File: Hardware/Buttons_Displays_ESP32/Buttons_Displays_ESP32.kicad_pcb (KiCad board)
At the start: 2 copper layers, 24 parts, among them J1 1778612, J2 1778612, J3 1778612, J4 1778612, J5 i2c, J6 USB_C_Receptacle_USB2.0_16P, SW1 SW_Push, SW2 SW_Push, U1 ESP32-S3-WROOM-1, U2 USBLC6-2P6

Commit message: pcb schermpjes af
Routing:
- net sda: track 14.4 -> 31.5 mm, vias 1 -> 2
- net scl: track 13.8 -> 25.0 mm, vias 1 -> 2
- net GPIO4: track 40.4 -> 29.3 mm, vias 1 -> 2
- net GND: track 0.00 -> 1.19 mm, vias 0 -> 142

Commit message: kleine aanpassingen
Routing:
- net GND: vias 142 -> 138
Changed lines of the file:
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@@
-	)
-	(via
-		(at 158.5 88.11)
-		(size 0.6)
-		(drill 0.3)
-		(layers "F.Cu" "B.Cu")
-		(free yes)
-		(net 2)
 	)
 	(via
@@
 	)
 	(via
-		(at 158.55 89.89)
-		(size 0.6)
-		(drill 0.3)
-		(layers "F.Cu" "B.Cu")
-		(free yes)
-		(net 2)
-	)
-	(via
 		(at 159.75 86.86)
 		(size 0.6)
@@
 	)
 	(via
-		(at 158.55 92.39)
-		(size 0.6)
-		(drill 0.3)
-		(layers "F.Cu" "B.Cu")
-		(free yes)
-		(net 2)
-	)
-	(via
 		(at 153.5 93.75)
 		(size 0.6)
@@
 		(size 0.6)
 		(drill 0.3)
-		(layers "F.Cu" "B.Cu")
-		(free yes)
-		(net 2)
-	)
-	(via
-		(at 158.5 85.61)
-		(size 0.6)
-		(drill 0.3)

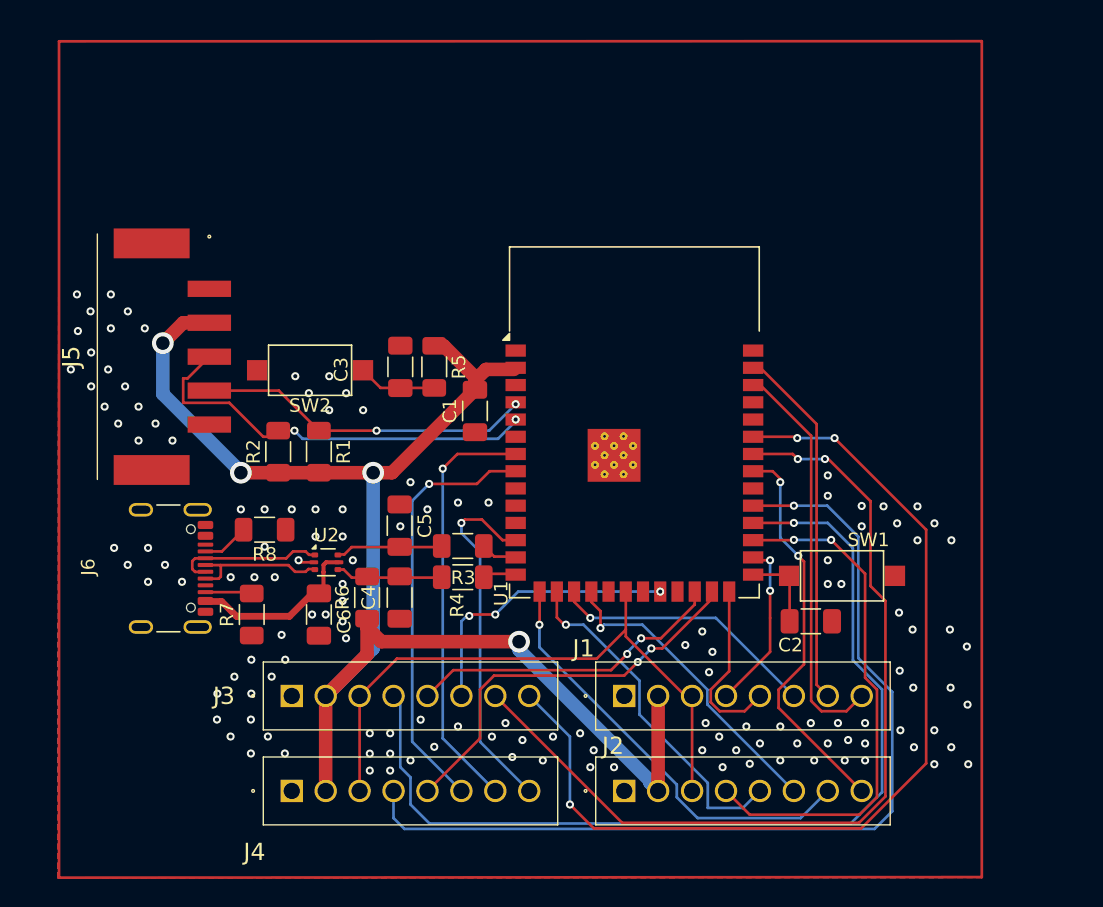
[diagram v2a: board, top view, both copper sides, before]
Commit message: mounting holes
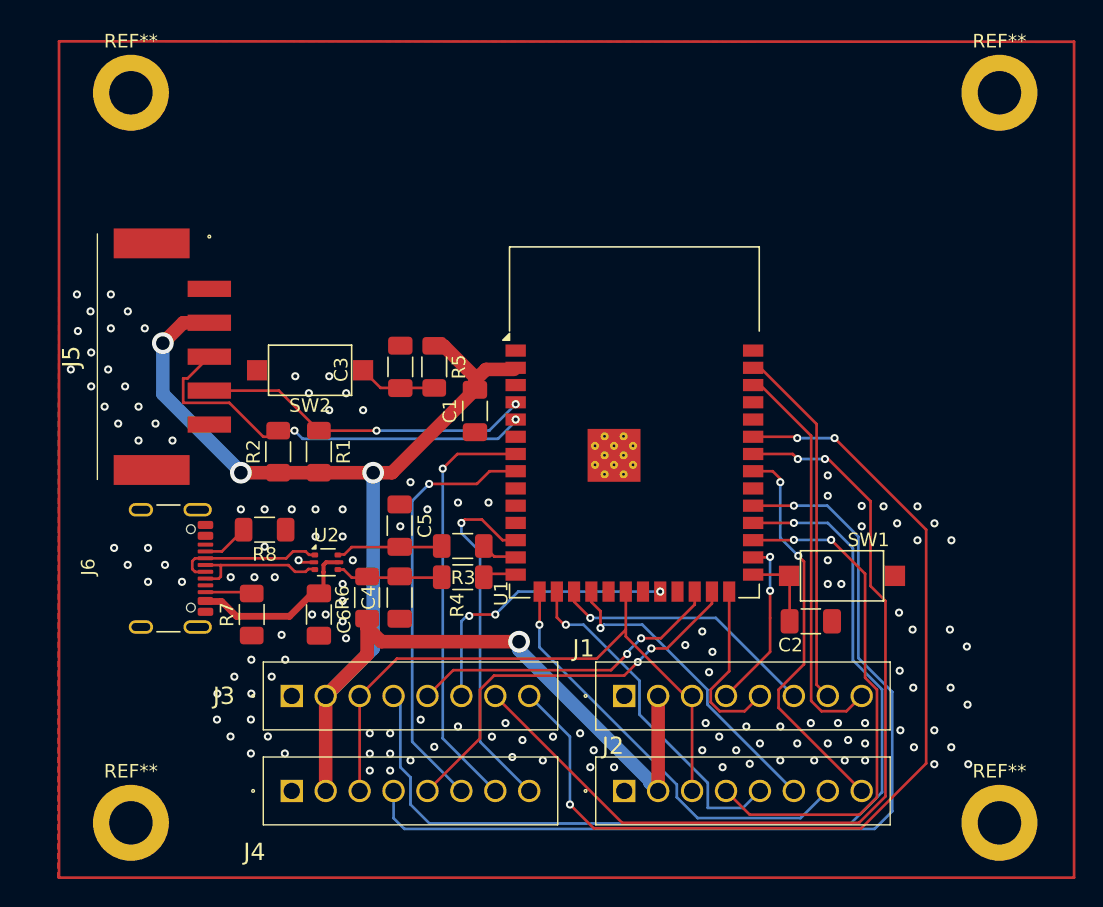
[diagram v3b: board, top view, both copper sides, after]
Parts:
- added REF**: MountingHole_3.2mm_M3_DIN965_Pad, MountingHole:MountingHole_3.2mm_M3_DIN965_Pad, F.Cu at (163.4, 101.1)
- added REF**: MountingHole_3.2mm_M3_DIN965_Pad, MountingHole:MountingHole_3.2mm_M3_DIN965_Pad, F.Cu at (163.4, 47.3)
- added REF**: MountingHole_3.2mm_M3_DIN965_Pad, MountingHole:MountingHole_3.2mm_M3_DIN965_Pad, F.Cu at (99.4, 47.3)
- added REF**: MountingHole_3.2mm_M3_DIN965_Pad, MountingHole:MountingHole_3.2mm_M3_DIN965_Pad, F.Cu at (99.4, 101.1)

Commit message: Update Buttons_Displays_ESP32.kicad_pcb
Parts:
- moved REF** 0.30 mm to (163.7, 101.1)
- moved REF** 0.30 mm to (163.7, 47.3)
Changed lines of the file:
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@@
 	(footprint "MountingHole:MountingHole_3.2mm_M3_DIN965_Pad"
 		(layer "F.Cu")
-		(at 163.4 101.1)
+		(at 163.7 101.1)
 		(descr "Mounting Hole 3.2mm, M3, DIN965")
 		(tags "mounting hole 3.2mm m3 din965")
@@
 			(at 0 -3.8 0)
 			(layer "F.SilkS")
+			(hide yes)
 			(effects
 				(font
@@
 	(footprint "MountingHole:MountingHole_3.2mm_M3_DIN965_Pad"
 		(layer "F.Cu")
-		(at 163.4 47.3)
+		(at 163.7 47.3)
 		(descr "Mounting Hole 3.2mm, M3, DIN965")
 		(tags "mounting hole 3.2mm m3 din965")
@@
 			(at 0 -3.8 0)
 			(layer "F.SilkS")
+			(hide yes)
 			(effects
 				(font
@@
 			(at 0 -3.8 0)
 			(layer "F.SilkS")
+			(hide yes)
 			(effects
 				(font
@@
 			(at 0 -3.8 0)
 			(layer "F.SilkS")
+			(hide yes)
 			(effects
 				(font
@@
 	)
 	(gr_line
-		(start 168.900024 43.54)
+		(start 94 105.18)
 		(end 94.1 43.51)
 		(stroke
@@
 	)
 	(gr_line
-		(start 94.1 105.14)
+		(start 168.900024 43.54)
 		(end 168.900024 105.14)
 		(stroke
@@
 	)
 	(gr_line
-		(start 168.900024 105.14)
+		(start 94.1 43.51)
 		(end 168.900024 43.54)
 		(stroke
@@
 	)
 	(gr_line
-		(start 94.1 43.51)
-		(end 94.1 105.14)
+		(start 168.900024 105.14)
+		(end 94 105.18)
 		(stroke
 			(width 0.2)

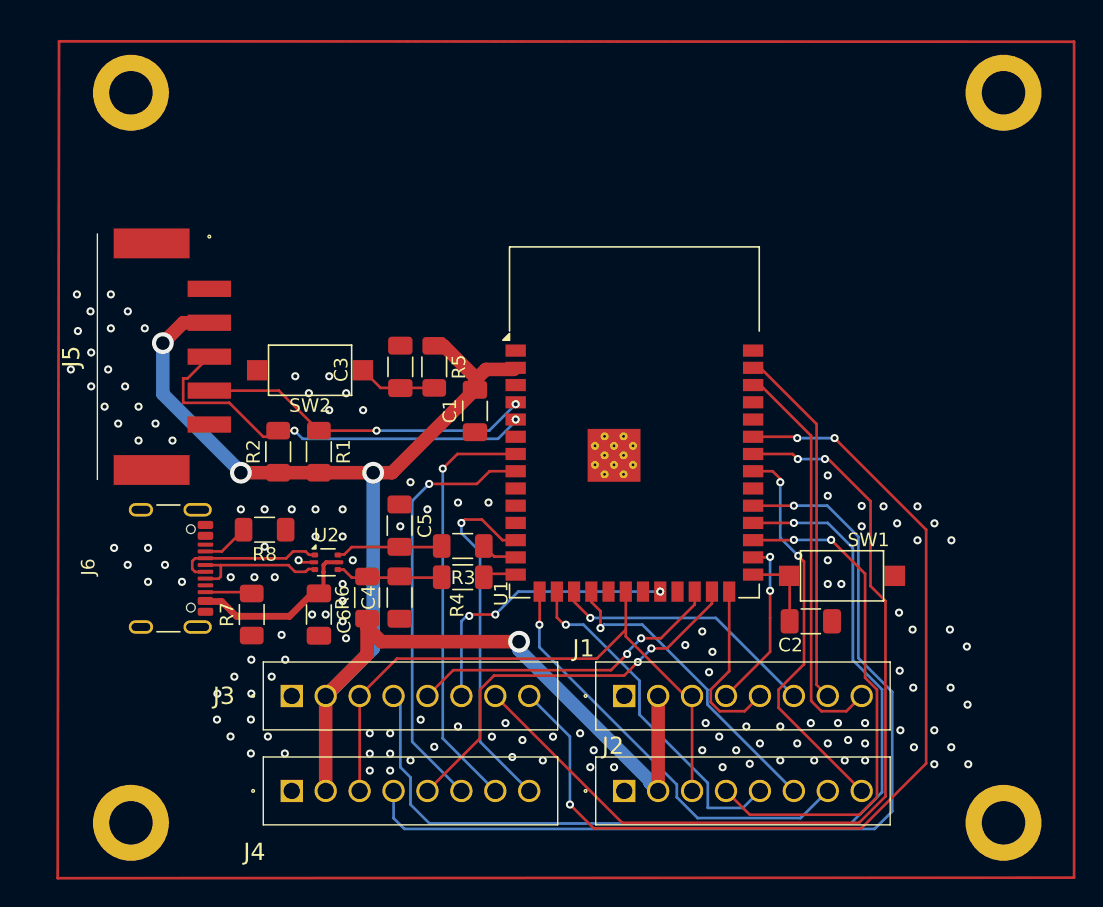
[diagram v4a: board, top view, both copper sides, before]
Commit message: pcb outlines
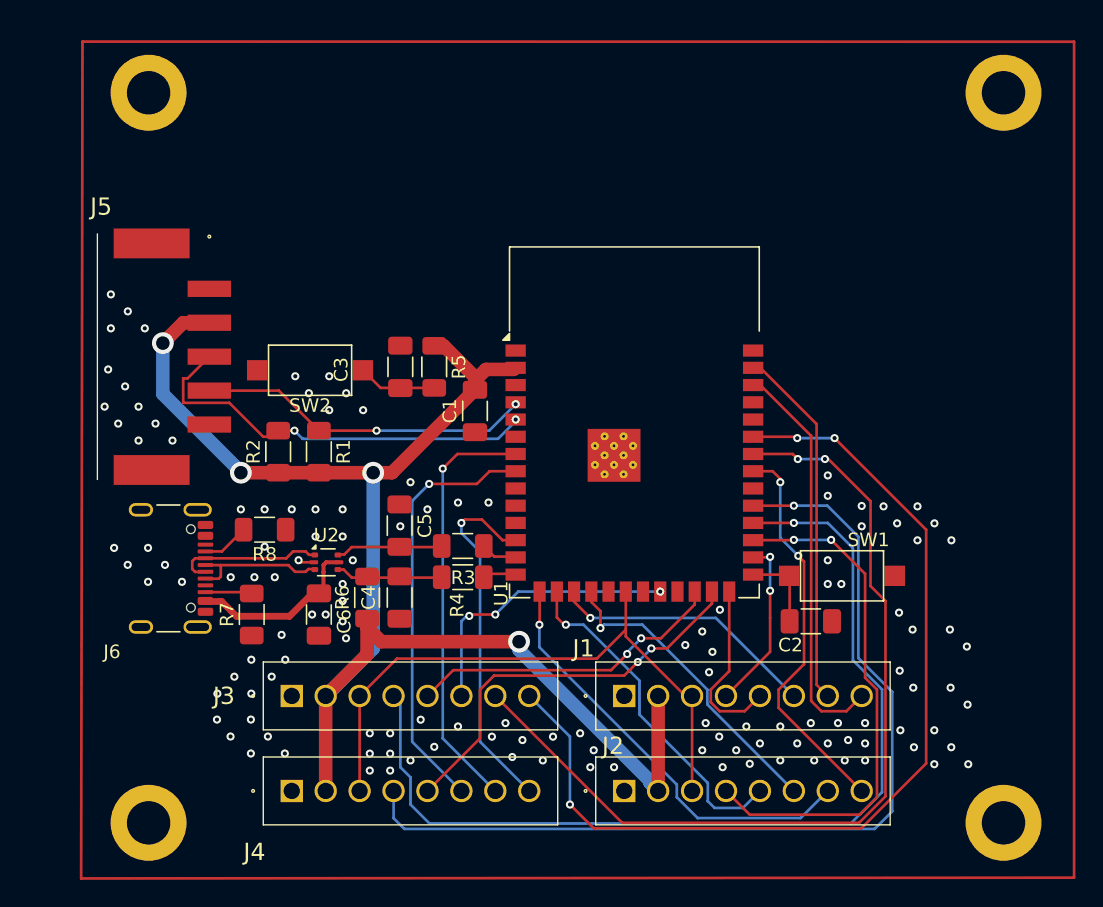
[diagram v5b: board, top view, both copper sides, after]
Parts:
- moved REF** 1.30 mm to (100.7, 47.3)
- moved REF** 1.30 mm to (100.7, 101.1)
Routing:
- net GND: vias 138 -> 133
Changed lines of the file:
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@@
 		(tags "Connector")
 		(property "Reference" "J5"
-			(at 0 10.175 90)
+			(at -11.05 7.975 180)
 			(layer "F.SilkS")
 			(effects
@@
 			(at 0 3.8 0)
 			(layer "F.Fab")
+			(hide yes)
 			(effects
 				(font
@@
 			(at 0 3.8 0)
 			(layer "F.Fab")
+			(hide yes)
 			(effects
 				(font
@@
 	(footprint "MountingHole:MountingHole_3.2mm_M3_DIN965_Pad"
 		(layer "F.Cu")
-		(at 99.4 47.3)
+		(at 100.7 47.3)
 		(descr "Mounting Hole 3.2mm, M3, DIN965")
 		(tags "mounting hole 3.2mm m3 din965")
@@
 			(at 0 3.8 0)
 			(layer "F.Fab")
+			(hide yes)
 			(effects
 				(font
@@
 	(footprint "MountingHole:MountingHole_3.2mm_M3_DIN965_Pad"
 		(layer "F.Cu")
-		(at 99.4 101.1)
+		(at 100.7 101.1)
 		(descr "Mounting Hole 3.2mm, M3, DIN965")
 		(tags "mounting hole 3.2mm m3 din965")
@@
 			(at 0 3.8 0)
 			(layer "F.Fab")
+			(hide yes)
 			(effects
 				(font
@@
 		(tags "USB C Type-C Receptacle SMD USB 2.0 16P 16C USB4105-15-A USB4105-15-A-060 USB4105-15-A-120 USB4105-GF-A USB4105-GF-A-060 USB4105-GF-A-120")
 		(property "Reference" "J6"
-			(at -0.1 4.96 90)
+			(at 6.15 3.21 0)
 			(unlocked yes)
 			(layer "F.SilkS")
@@
 			(unlocked yes)
 			(layer "F.Fab")
+			(hide yes)
 			(effects
 				(font
@@
 	)
 	(gr_line
-		(start 94 105.18)
-		(end 94.1 43.51)
+		(start 95.73 105.2)
+		(end 95.83 43.53)
 		(stroke
 			(width 0.2)
@@
 	)
 	(gr_line
-		(start 94.1 43.51)
+		(start 95.83 43.53)
 		(end 168.900024 43.54)
 		(stroke
@@
 	(gr_line
 		(start 168.900024 105.14)
-		(end 94 105.18)
+		(end 95.73 105.2)
 		(stroke
 			(width 0.2)
@@
 	)
 	(via
-		(at 96.47 68.94)
-		(size 0.6)
-		(drill 0.3)
-		(layers "F.Cu" "B.Cu")
-		(free yes)
-		(net 2)
-	)
-	(via
 		(at 154.86 77.78)
 		(size 0.6)
@@
 	)
 	(via
-		(at 96.47 66.44)
-		(size 0.6)
-		(drill 0.3)
-		(layers "F.Cu" "B.Cu")
-		(free yes)
-		(net 2)
-	)
-	(via
 		(at 153.25 77.75)
 		(size 0.6)
@@
 	)
 	(via
-		(at 95.49 64.86)
-		(size 0.6)
-		(drill 0.3)
-		(layers "F.Cu" "B.Cu")
-		(free yes)
-		(net 2)
-	)
-	(via
 		(at 141.75 93.75)
 		(size 0.6)
@@
 	)
 	(via
-		(at 95.42 62.16)
-		(size 0.6)
-		(drill 0.3)
-		(layers "F.Cu" "B.Cu")
-		(free yes)
-		(net 2)
-	)
-	(via
 		(at 153.5 93.75)
 		(size 0.6)
@@
 	)
 	(via
-		(at 96.42 63.41)
-		(size 0.6)
-		(drill 0.3)
-		(layers "F.Cu" "B.Cu")
-		(free yes)
-		(net 2)
-	)
-	(via
 		(at 103.16 83.34)
 		(size 0.6)
@@
 	)
 	(via
-		(at 94.97 67.69)
-		(size 0.6)
-		(drill 0.3)
-		(layers "F.Cu" "B.Cu")
-		(free yes)
-		(net 2)
-	)
-	(via
 		(at 156 85.61)
 		(size 0.6)
@@
 		(net 2)
 	)
+	(via
+		(at 142.8 85.4)
+		(size 0.6)
+		(drill 0.3)
+		(layers "F.Cu" "B.Cu")
+		(free yes)
+		(net 2)
+	)
 	(segment
 		(start 147.9375 86.25)
@@
 	)
 	(segment
-		(start 136.875 93.125)
-		(end 141.906677 98.156677)
+		(start 141.906677 98.156677)
+		(end 141.906677 99.506677)
 		(width 0.2)
 		(layer "B.Cu")
@@
 	)
 	(segment
-		(start 144.5 100)
-		(end 145.75 98.75)
+		(start 136.875 90.625)
+		(end 136.875 93.125)
 		(width 0.2)
 		(layer "B.Cu")
@@
 	)
 	(segment
-		(start 141.906677 100)
+		(start 142.4 100)
 		(end 144.5 100)
 		(width 0.2)
@@
 	)
 	(segment
+		(start 144.5 100)
+		(end 145.75 98.75)
+		(width 0.2)
+		(layer "B.Cu")
+		(net 26)
+	)
+	(segment
 		(start 132.75 86.5)
 		(end 136.875 90.625)
@@
 	)
 	(segment
-		(start 131.450003 86.5)
-		(end 132.75 86.5)
+		(start 136.875 93.125)
+		(end 141.906677 98.156677)
 		(width 0.2)
 		(layer "B.Cu")
@@
 	)
 	(segment
-		(start 136.875 90.625)
-		(end 136.875 93.125)
+		(start 141.906677 99.506677)
+		(end 142.4 100)
 		(width 0.2)
 		(layer "B.Cu")
@@
 	)
 	(segment
-		(start 141.906677 98.156677)
-		(end 141.906677 100)
+		(start 131.450003 86.5)
+		(end 132.75 86.5)
 		(width 0.2)
 		(layer "B.Cu")
@@
 		(polygon
 			(pts
-				(xy 168.900024 43.54) (xy 168.900024 105.14) (xy 94 105.18) (xy 94.1 43.51)
+				(xy 168.900024 43.54) (xy 168.900024 105.14) (xy 95.73 105.2) (xy 95.83 43.53)
 			)
 		)
